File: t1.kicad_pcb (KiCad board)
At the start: 4 copper layers, 63 x 35.6 mm, 47 parts, among them J1 Barrel_Jack_Switch, J2 USB_B, J3 P1, J4 2x2M, J5 ICSP1, J6 P2, U1 ATmega8U2-AU, Y1 16MHz

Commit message: Fixed PCB parity
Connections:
- U1 pad 14: Net-(U1-Pad14) -> unconnected-(U1-PB0-Pad14)

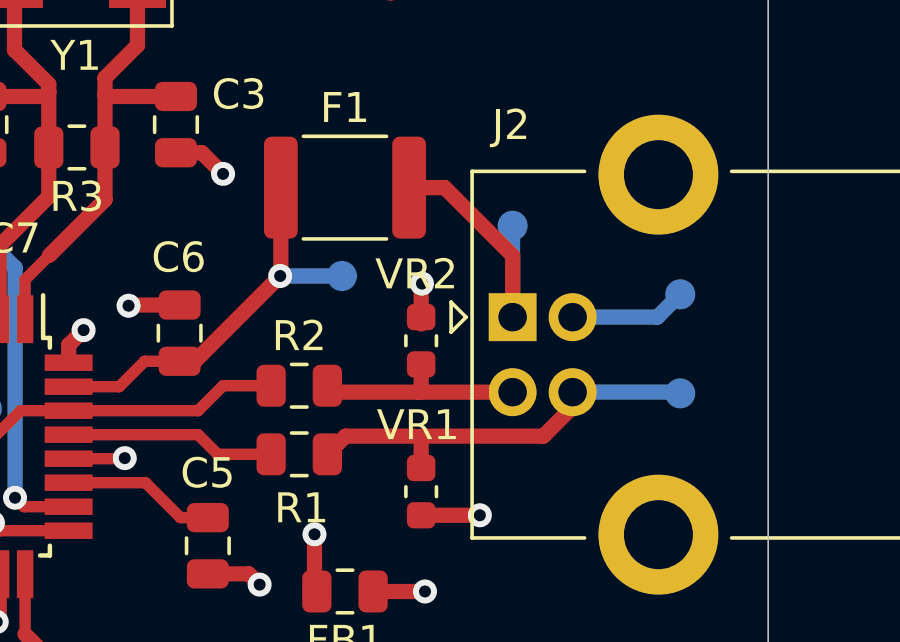
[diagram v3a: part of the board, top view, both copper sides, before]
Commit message: Migrated to KiCad 9 for tests
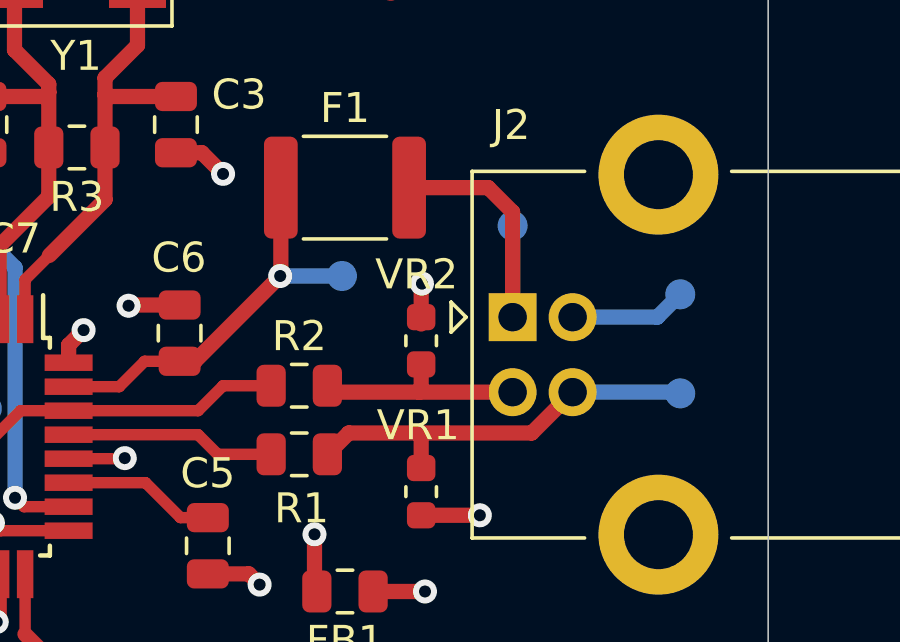
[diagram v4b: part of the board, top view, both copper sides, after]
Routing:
- net Net-(J2-VBUS): track 9.49 -> 10.3 mm
